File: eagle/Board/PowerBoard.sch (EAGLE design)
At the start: 19 parts, among them J1 JACK-PLUG0, Q1 2SA1020L-Y, Q2 2SK3234, U1 MC34063AP1

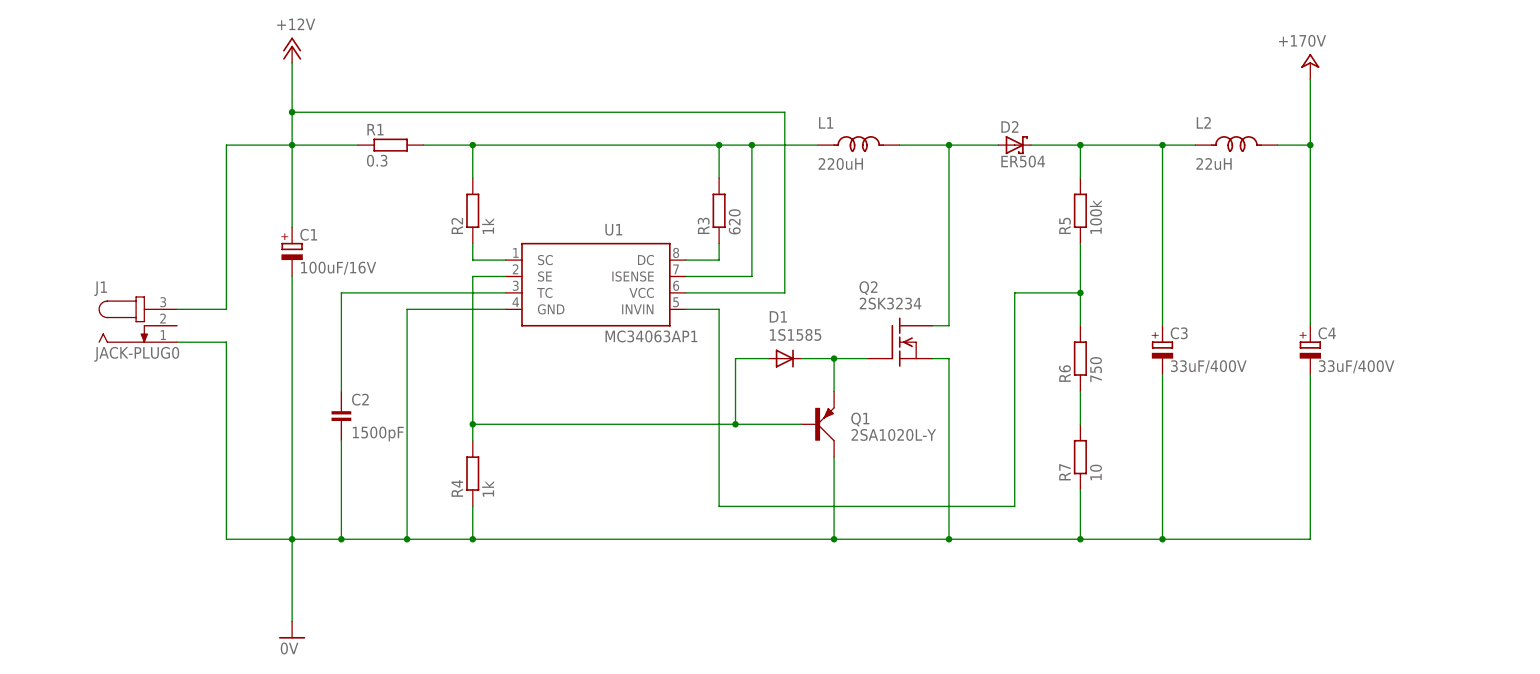
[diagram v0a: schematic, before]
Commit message: 170V出力をターミナルブロックに変更
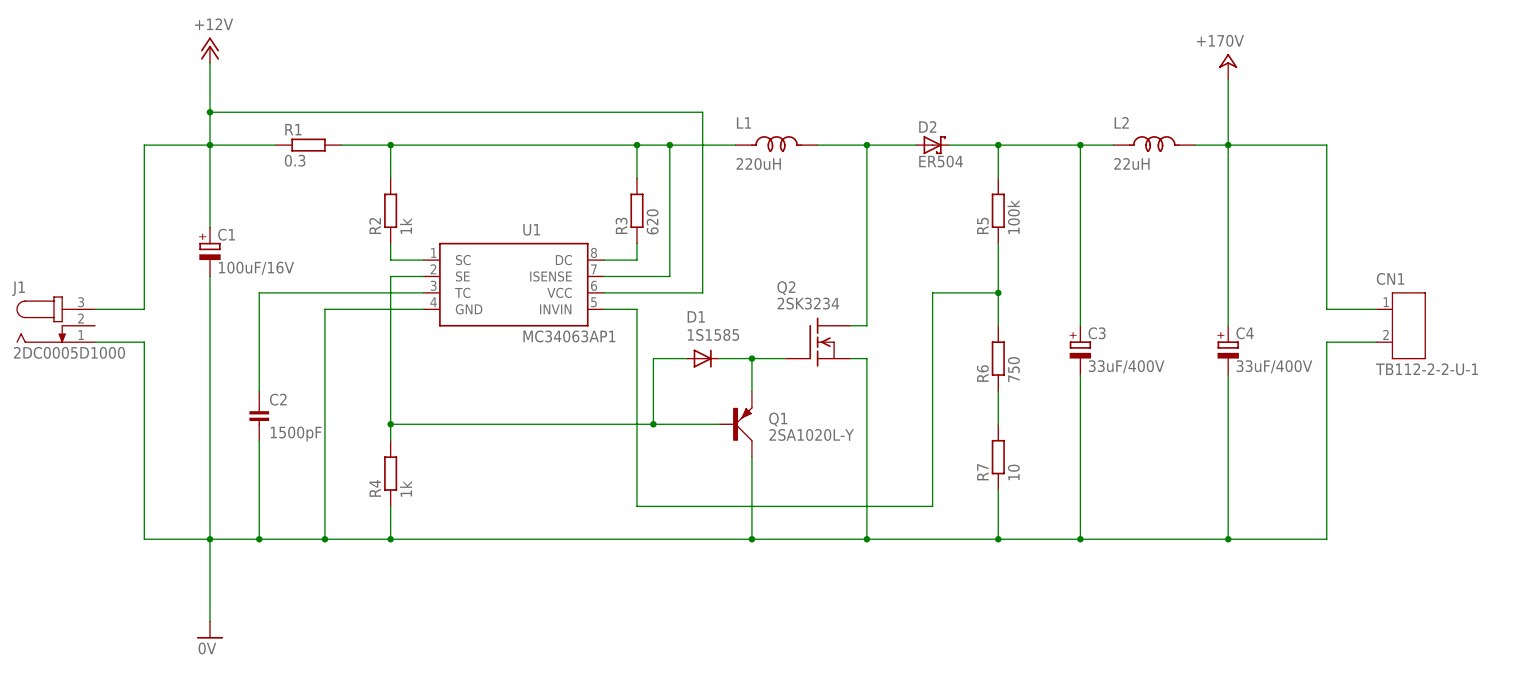
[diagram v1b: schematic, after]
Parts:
- added CN1: TB112-2-2-U-1, Connectors:TB112-2-2-U-1
- J1: value JACK-PLUG0 -> 2DC0005D1000; device Connectors:JACK-PLUG0 -> Connectors:2DC0005D1000
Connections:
- net +24V: now also CN1.1
- net 0V: now also CN1.2
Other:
- moved on the sheet: C1, C2, C3, C4, D1, D2, J1, L1, L2, Q1, Q2, R1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
